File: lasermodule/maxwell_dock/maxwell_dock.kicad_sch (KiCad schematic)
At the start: 2 parts

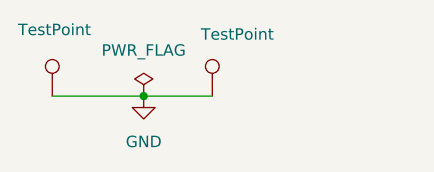
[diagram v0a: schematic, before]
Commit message: maxwell lock updated, magnets cutouts improved
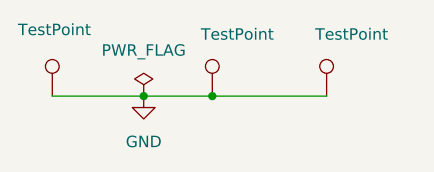
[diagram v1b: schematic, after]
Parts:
- added TP3: TestPoint, footprints:TestPoint_Pad_D8.0mm, symbol Connector:TestPoint
- TP1, TP2: footprint TestPoint:TestPoint_Pad_1.0x1.0mm -> footprints:TestPoint_Pad_D8.0mm
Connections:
- net GND: now also TP3.1
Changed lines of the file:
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@@
 	(paper "A4")
+	(junction
+		(at 157.48 104.14)
+		(diameter 0)
+		(color 0 0 0 0)
+	)
 	(junction
 		(at 149.86 104.14)
 		(diameter 0)
 		(color 0 0 0 0)
+	)
+	(wire
+		(pts
+			(xy 157.48 104.14) (xy 170.18 104.14)
+		)
+		(stroke
+			(width 0)
+			(type default)
+		)
 	)
 	(wire
@@
 			)
 		)
-		(property "Footprint" "TestPoint:TestPoint_Pad_1.0x1.0mm"
+		(property "Footprint" "footprints:TestPoint_Pad_D8.0mm"
 			(at 144.78 104.14 0)
 			(hide yes)
@@
 				(path "/98b9016e-8416-4cda-9c12-90a66aaf6514"
 					(reference "TP2")
+					(unit 1)
+				)
+			)
+		)
+	)
+	(symbol
+		(lib_id "Connector:TestPoint")
+		(at 170.18 104.14 0)
+		(unit 1)
+		(body_style 1)
+		(exclude_from_sim no)
+		(in_bom yes)
+		(on_board yes)
+		(in_pos_files yes)
+		(dnp no)
+		(property "Reference" "TP3"
+			(at 172.72 99.5679 0)
+			(hide yes)
+			(show_name no)
+			(do_not_autoplace no)
+			(effects
+				(font
+					(size 1.27 1.27)
+				)
+				(justify left)
+			)
+		)
+		(property "Value" "TestPoint"
+			(at 168.91 97.282 0)
+			(show_name no)
+			(do_not_autoplace no)
+			(effects
+				(font
+					(size 1.27 1.27)
+				)
+				(justify left)
+			)
+		)
+		(property "Footprint" "footprints:TestPoint_Pad_D8.0mm"
+			(at 175.26 104.14 0)
+			(hide yes)
+			(show_name no)
+			(do_not_autoplace no)
+			(effects
+				(font
+					(size 1.27 1.27)
+				)
+			)
+		)
+		(property "Datasheet" ""
+			(at 175.26 104.14 0)
+			(hide yes)
+			(show_name no)
+			(do_not_autoplace no)
+			(effects
+				(font
+					(size 1.27 1.27)
+				)
+			)
+		)
+		(property "Description" "test point"
+			(at 170.18 104.14 0)
+			(hide yes)
+			(show_name no)
+			(do_not_autoplace no)
+			(effects
+				(font
+					(size 1.27 1.27)
+				)
+			)
+		)
+		(pin "1"
+		)
+		(instances
+			(project "maxwell_dock"
+				(path "/98b9016e-8416-4cda-9c12-90a66aaf6514"
+					(reference "TP3")
 					(unit 1)
 				)
@@
 			)
 		)
-		(property "Footprint" "TestPoint:TestPoint_Pad_1.0x1.0mm"
+		(property "Footprint" "footprints:TestPoint_Pad_D8.0mm"
 			(at 162.56 104.14 0)
 			(hide yes)
